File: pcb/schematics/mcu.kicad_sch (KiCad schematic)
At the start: 25 parts, among them J3 Conn_01x06_Female, SW2 Reset, U3 STM32F103V8Tx, Y2 24MHz

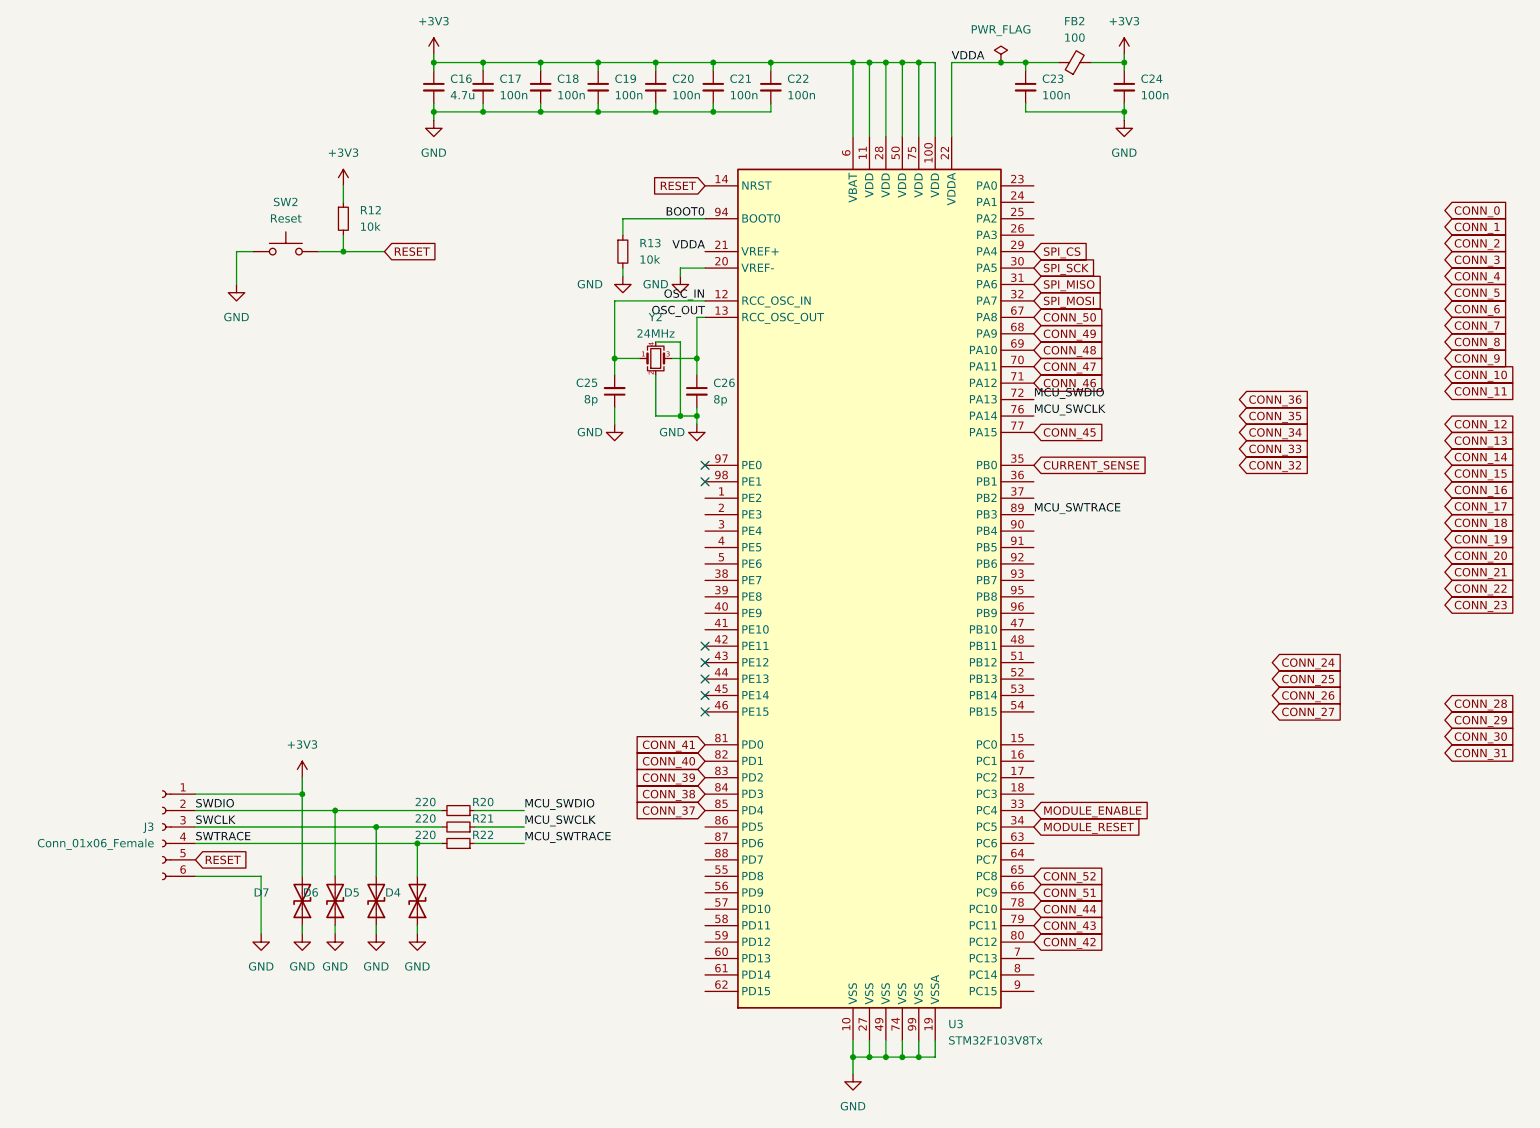
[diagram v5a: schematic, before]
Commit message: route more data traces
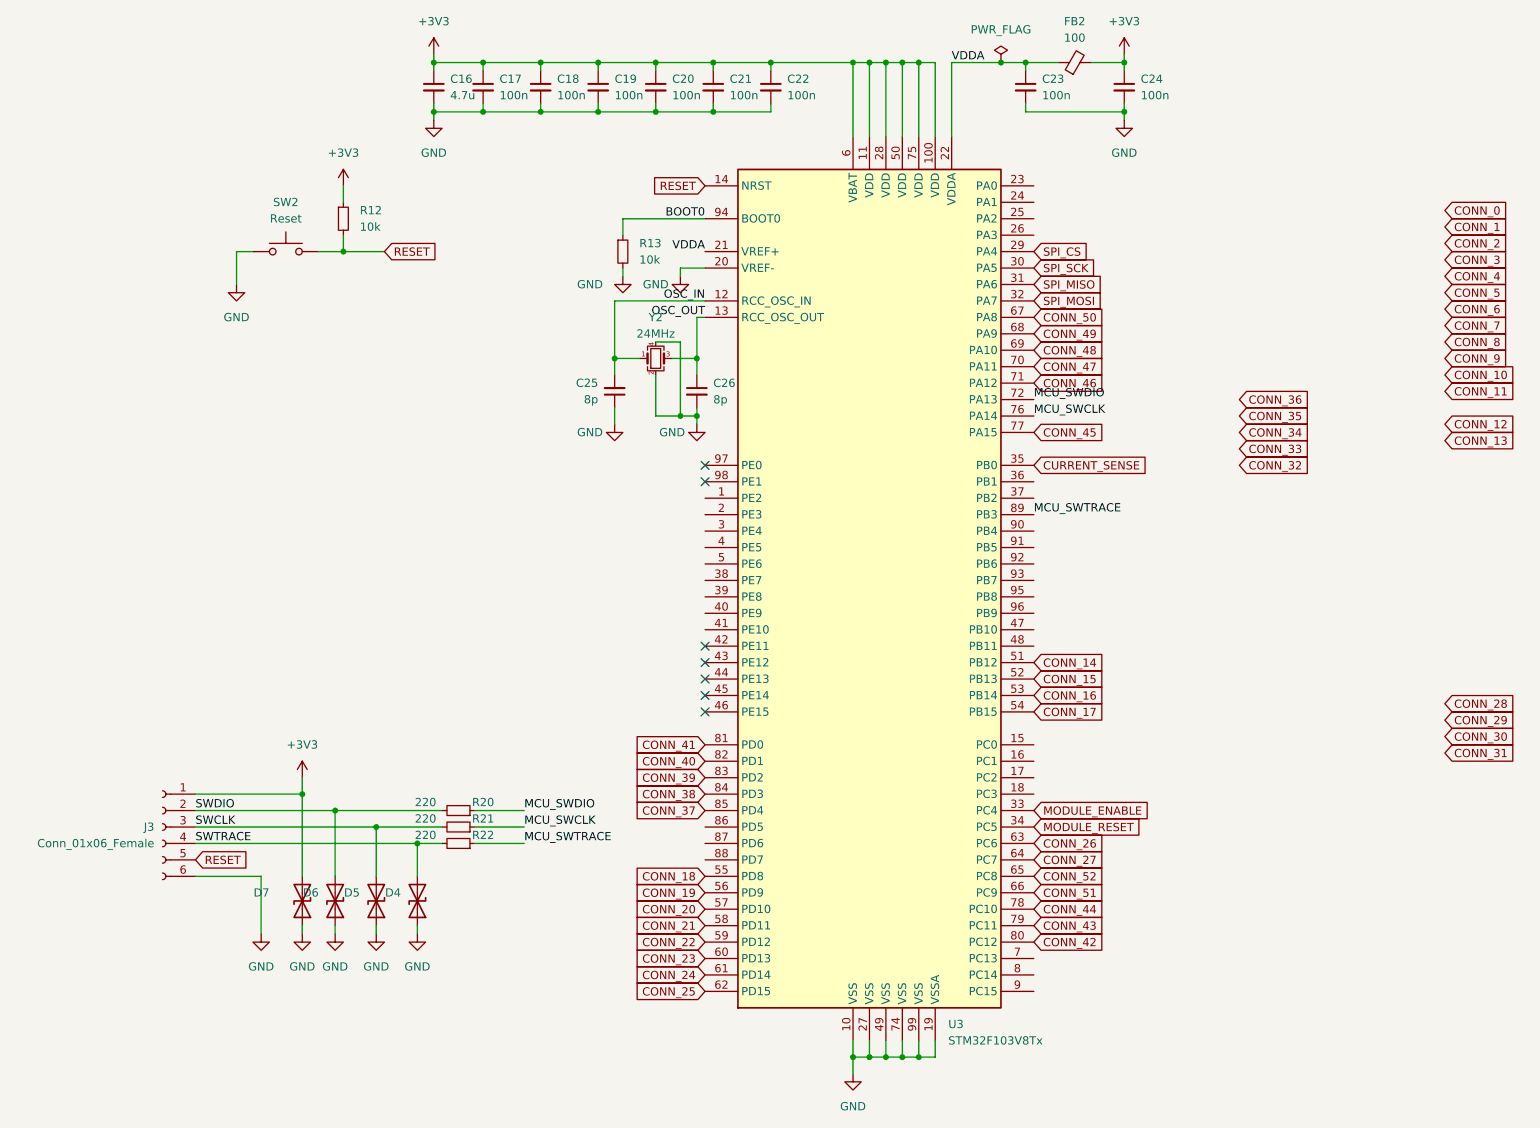
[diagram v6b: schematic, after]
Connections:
- net CONN_14: now also U3.51 (PB12)
- net CONN_15: now also U3.52 (PB13)
- net CONN_16: now also U3.53 (PB14)
- net CONN_17: now also U3.54 (PB15)
- net CONN_18: now also U3.55 (PD8)
- net CONN_19: now also U3.56 (PD9)
- net CONN_20: now also U3.57 (PD10)
- net CONN_21: now also U3.58 (PD11)
- net CONN_22: now also U3.59 (PD12)
- net CONN_23: now also U3.60 (PD13)
- net CONN_24: now also U3.61 (PD14)
- net CONN_25: now also U3.62 (PD15)
- net CONN_26: now also U3.63 (PC6)
- net CONN_27: now also U3.64 (PC7)
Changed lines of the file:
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@@
     )
   )
-  (global_label "CONN_21" (shape input) (at 236.22 106.68 0)
-    (effects (font (size 1.27 1.27)) (justify left))
-    (property "Intersheet References" "${INTERSHEET_REFS}" (id 0) (at 248.5512 106.6006 0)
-      (effects (font (size 1.27 1.27)) (justify left))
-    )
-  )
-  (global_label "CONN_26" (shape input) (at 209.55 125.73 0)
-    (effects (font (size 1.27 1.27)) (justify left))
-    (property "Intersheet References" "${INTERSHEET_REFS}" (id 0) (at 221.8812 125.6506 0)
+  (global_label "CONN_21" (shape input) (at 121.92 161.29 180)
+    (effects (font (size 1.27 1.27)) (justify right))
+    (property "Intersheet References" "${INTERSHEET_REFS}" (id 0) (at 109.5888 161.2106 0)
+      (effects (font (size 1.27 1.27)) (justify right))
+    )
+  )
+  (global_label "CONN_26" (shape input) (at 172.72 148.59 0)
+    (effects (font (size 1.27 1.27)) (justify left))
+    (property "Intersheet References" "${INTERSHEET_REFS}" (id 0) (at 185.0512 148.5106 0)
       (effects (font (size 1.27 1.27)) (justify left))
     )
@@
     )
   )
-  (global_label "CONN_17" (shape input) (at 236.22 96.52 0)
-    (effects (font (size 1.27 1.27)) (justify left))
-    (property "Intersheet References" "${INTERSHEET_REFS}" (id 0) (at 248.5512 96.4406 0)
+  (global_label "CONN_17" (shape input) (at 172.72 128.27 0)
+    (effects (font (size 1.27 1.27)) (justify left))
+    (property "Intersheet References" "${INTERSHEET_REFS}" (id 0) (at 185.0512 128.1906 0)
       (effects (font (size 1.27 1.27)) (justify left))
     )
@@
     )
   )
-  (global_label "CONN_18" (shape input) (at 236.22 99.06 0)
-    (effects (font (size 1.27 1.27)) (justify left))
-    (property "Intersheet References" "${INTERSHEET_REFS}" (id 0) (at 248.5512 98.9806 0)
-      (effects (font (size 1.27 1.27)) (justify left))
-    )
-  )
-  (global_label "CONN_23" (shape input) (at 236.22 111.76 0)
-    (effects (font (size 1.27 1.27)) (justify left))
-    (property "Intersheet References" "${INTERSHEET_REFS}" (id 0) (at 248.5512 111.6806 0)
-      (effects (font (size 1.27 1.27)) (justify left))
-    )
-  )
-  (global_label "CONN_19" (shape input) (at 236.22 101.6 0)
-    (effects (font (size 1.27 1.27)) (justify left))
-    (property "Intersheet References" "${INTERSHEET_REFS}" (id 0) (at 248.5512 101.5206 0)
-      (effects (font (size 1.27 1.27)) (justify left))
+  (global_label "CONN_18" (shape input) (at 121.92 153.67 180)
+    (effects (font (size 1.27 1.27)) (justify right))
+    (property "Intersheet References" "${INTERSHEET_REFS}" (id 0) (at 109.5888 153.5906 0)
+      (effects (font (size 1.27 1.27)) (justify right))
+    )
+  )
+  (global_label "CONN_23" (shape input) (at 121.92 166.37 180)
+    (effects (font (size 1.27 1.27)) (justify right))
+    (property "Intersheet References" "${INTERSHEET_REFS}" (id 0) (at 109.5888 166.2906 0)
+      (effects (font (size 1.27 1.27)) (justify right))
+    )
+  )
+  (global_label "CONN_19" (shape input) (at 121.92 156.21 180)
+    (effects (font (size 1.27 1.27)) (justify right))
+    (property "Intersheet References" "${INTERSHEET_REFS}" (id 0) (at 109.5888 156.1306 0)
+      (effects (font (size 1.27 1.27)) (justify right))
     )
   )
@@
     )
   )
-  (global_label "CONN_24" (shape input) (at 209.55 120.65 0)
-    (effects (font (size 1.27 1.27)) (justify left))
-    (property "Intersheet References" "${INTERSHEET_REFS}" (id 0) (at 221.8812 120.5706 0)
-      (effects (font (size 1.27 1.27)) (justify left))
+  (global_label "CONN_24" (shape input) (at 121.92 168.91 180)
+    (effects (font (size 1.27 1.27)) (justify right))
+    (property "Intersheet References" "${INTERSHEET_REFS}" (id 0) (at 109.5888 168.8306 0)
+      (effects (font (size 1.27 1.27)) (justify right))
     )
   )
@@
     )
   )
-  (global_label "CONN_20" (shape input) (at 236.22 104.14 0)
-    (effects (font (size 1.27 1.27)) (justify left))
-    (property "Intersheet References" "${INTERSHEET_REFS}" (id 0) (at 248.5512 104.0606 0)
-      (effects (font (size 1.27 1.27)) (justify left))
+  (global_label "CONN_20" (shape input) (at 121.92 158.75 180)
+    (effects (font (size 1.27 1.27)) (justify right))
+    (property "Intersheet References" "${INTERSHEET_REFS}" (id 0) (at 109.5888 158.6706 0)
+      (effects (font (size 1.27 1.27)) (justify right))
     )
   )
@@
     )
   )
-  (global_label "CONN_15" (shape input) (at 236.22 91.44 0)
-    (effects (font (size 1.27 1.27)) (justify left))
-    (property "Intersheet References" "${INTERSHEET_REFS}" (id 0) (at 248.5512 91.3606 0)
+  (global_label "CONN_15" (shape input) (at 172.72 123.19 0)
+    (effects (font (size 1.27 1.27)) (justify left))
+    (property "Intersheet References" "${INTERSHEET_REFS}" (id 0) (at 185.0512 123.1106 0)
       (effects (font (size 1.27 1.27)) (justify left))
     )
@@
     )
   )
-  (global_label "CONN_16" (shape input) (at 236.22 93.98 0)
-    (effects (font (size 1.27 1.27)) (justify left))
-    (property "Intersheet References" "${INTERSHEET_REFS}" (id 0) (at 248.5512 93.9006 0)
+  (global_label "CONN_16" (shape input) (at 172.72 125.73 0)
+    (effects (font (size 1.27 1.27)) (justify left))
+    (property "Intersheet References" "${INTERSHEET_REFS}" (id 0) (at 185.0512 125.6506 0)
       (effects (font (size 1.27 1.27)) (justify left))
     )
@@
     )
   )
-  (global_label "CONN_22" (shape input) (at 236.22 109.22 0)
-    (effects (font (size 1.27 1.27)) (justify left))
-    (property "Intersheet References" "${INTERSHEET_REFS}" (id 0) (at 248.5512 109.1406 0)
-      (effects (font (size 1.27 1.27)) (justify left))
+  (global_label "CONN_22" (shape input) (at 121.92 163.83 180)
+    (effects (font (size 1.27 1.27)) (justify right))
+    (property "Intersheet References" "${INTERSHEET_REFS}" (id 0) (at 109.5888 163.7506 0)
+      (effects (font (size 1.27 1.27)) (justify right))
     )
   )
@@
     )
   )
-  (global_label "CONN_27" (shape input) (at 209.55 128.27 0)
-    (effects (font (size 1.27 1.27)) (justify left))
-    (property "Intersheet References" "${INTERSHEET_REFS}" (id 0) (at 221.8812 128.1906 0)
+  (global_label "CONN_27" (shape input) (at 172.72 151.13 0)
+    (effects (font (size 1.27 1.27)) (justify left))
+    (property "Intersheet References" "${INTERSHEET_REFS}" (id 0) (at 185.0512 151.0506 0)
       (effects (font (size 1.27 1.27)) (justify left))
     )
@@
     )
   )
-  (global_label "CONN_14" (shape input) (at 236.22 88.9 0)
-    (effects (font (size 1.27 1.27)) (justify left))
-    (property "Intersheet References" "${INTERSHEET_REFS}" (id 0) (at 248.5512 88.8206 0)
+  (global_label "CONN_14" (shape input) (at 172.72 120.65 0)
+    (effects (font (size 1.27 1.27)) (justify left))
+    (property "Intersheet References" "${INTERSHEET_REFS}" (id 0) (at 185.0512 120.5706 0)
       (effects (font (size 1.27 1.27)) (justify left))
     )
@@
     )
   )
-  (global_label "CONN_25" (shape input) (at 209.55 123.19 0)
-    (effects (font (size 1.27 1.27)) (justify left))
-    (property "Intersheet References" "${INTERSHEET_REFS}" (id 0) (at 221.8812 123.1106 0)
-      (effects (font (size 1.27 1.27)) (justify left))
-    )
-  )
+  (global_label "CONN_25" (shape input) (at 121.92 171.45 180)
+    (effects (font (size 1.27 1.27)) (justify right))
+    (property "Intersheet References" "${INTERSHEET_REFS}" (id 0) (at 109.5888 171.3706 0)
+      (effects (font (size 1.27 1.27)) (justify right))
+    )
+  )

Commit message: route more data traces
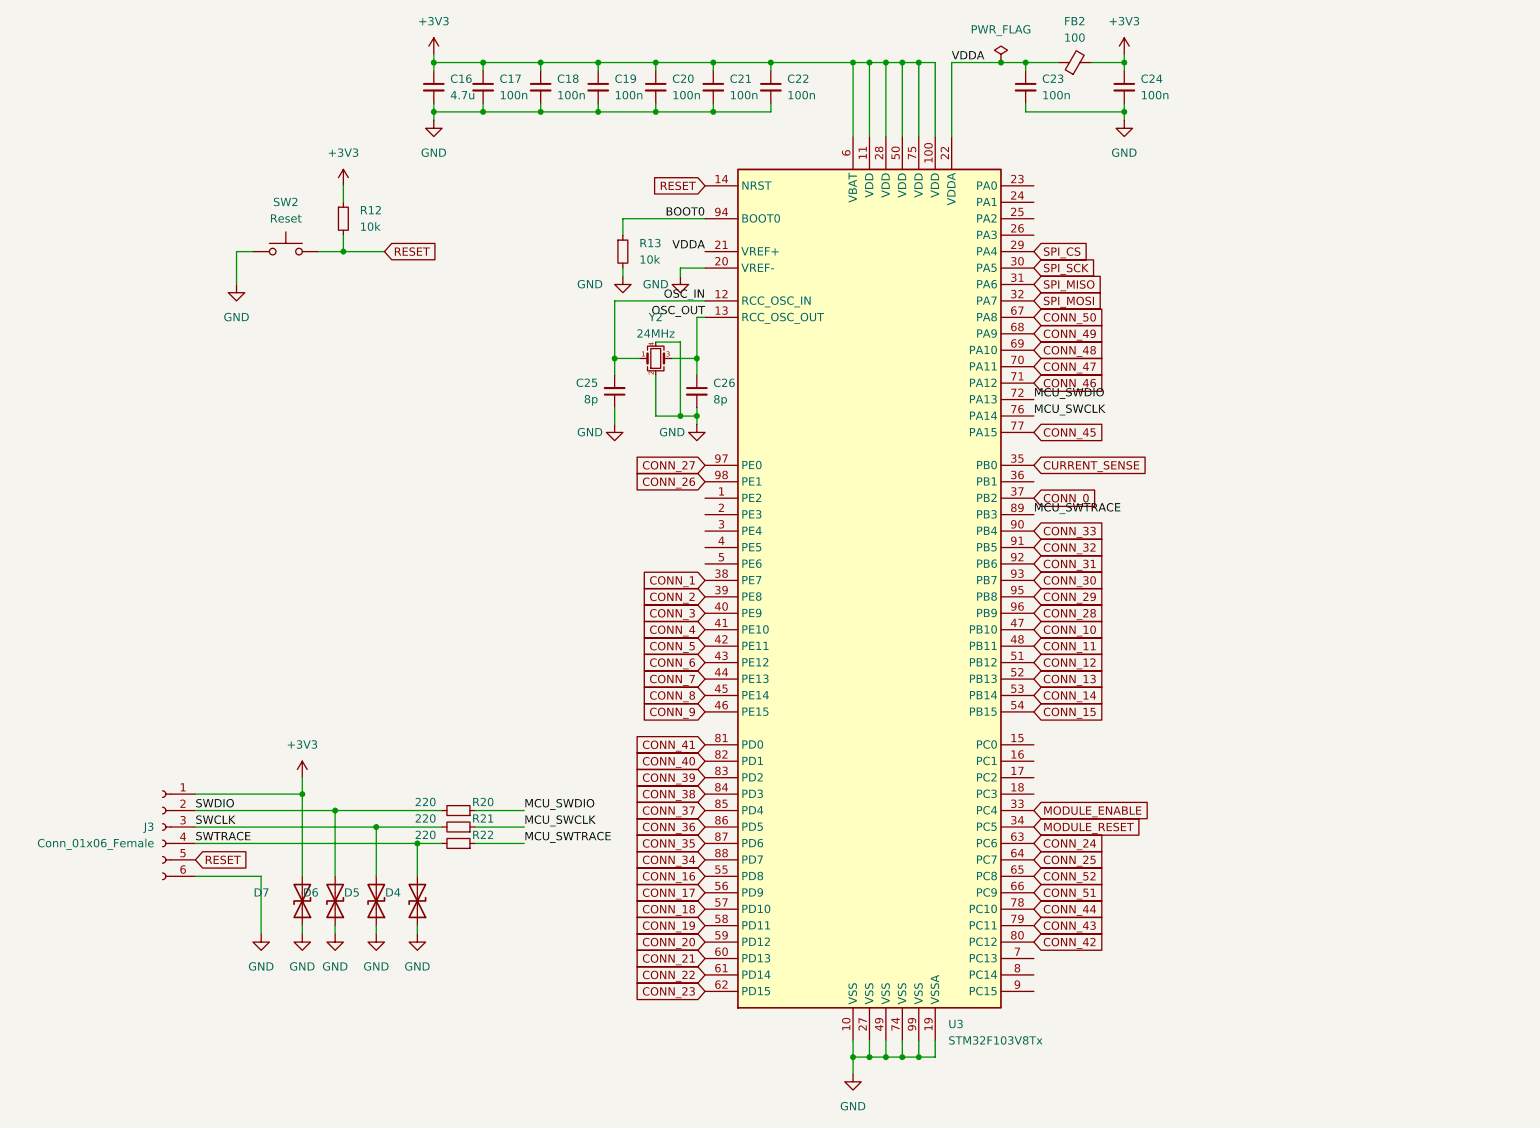
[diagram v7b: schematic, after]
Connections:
- net CONN_0: now also U3.37 (PB2)
- net CONN_1: now also U3.38 (PE7)
- net CONN_10: now also U3.47 (PB10)
- net CONN_11: now also U3.48 (PB11)
- net CONN_12: now also U3.51 (PB12)
- net CONN_13: now also U3.52 (PB13)
- net CONN_14: now also U3.53 (PB14); no longer U3.51 (PB12)
- net CONN_15: now also U3.54 (PB15); no longer U3.52 (PB13)
- net CONN_16: now also U3.55 (PD8); no longer U3.53 (PB14)
- net CONN_17: now also U3.56 (PD9); no longer U3.54 (PB15)
- net CONN_18: now also U3.57 (PD10); no longer U3.55 (PD8)
- net CONN_19: now also U3.58 (PD11); no longer U3.56 (PD9)
- net CONN_2: now also U3.39 (PE8)
- net CONN_20: now also U3.59 (PD12); no longer U3.57 (PD10)
- net CONN_21: now also U3.60 (PD13); no longer U3.58 (PD11)
- net CONN_22: now also U3.61 (PD14); no longer U3.59 (PD12)
- net CONN_23: now also U3.62 (PD15); no longer U3.60 (PD13)
- net CONN_24: now also U3.63 (PC6); no longer U3.61 (PD14)
- net CONN_25: now also U3.64 (PC7); no longer U3.62 (PD15)
- net CONN_26: now also U3.98 (PE1); no longer U3.63 (PC6)
- net CONN_27: now also U3.97 (PE0); no longer U3.64 (PC7)
- net CONN_28: now also U3.96 (PB9)
- net CONN_29: now also U3.95 (PB8)
- net CONN_3: now also U3.40 (PE9)
- net CONN_30: now also U3.93 (PB7)
- net CONN_31: now also U3.92 (PB6)
- net CONN_32: now also U3.91 (PB5)
- net CONN_33: now also U3.90 (PB4)
- net CONN_34: now also U3.88 (PD7)
- net CONN_35: now also U3.87 (PD6)
- net CONN_36: now also U3.86 (PD5)
- net CONN_4: now also U3.41 (PE10)
- net CONN_5: now also U3.42 (PE11)
- net CONN_6: now also U3.43 (PE12)
- net CONN_7: now also U3.44 (PE13)
- net CONN_8: now also U3.45 (PE14)
- net CONN_9: now also U3.46 (PE15)
- no-connect marks 7 -> 0
